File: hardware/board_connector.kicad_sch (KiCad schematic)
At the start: 3 parts, among them J6 61301611821, J7 PH1-08-UA, J8 PRT-09279

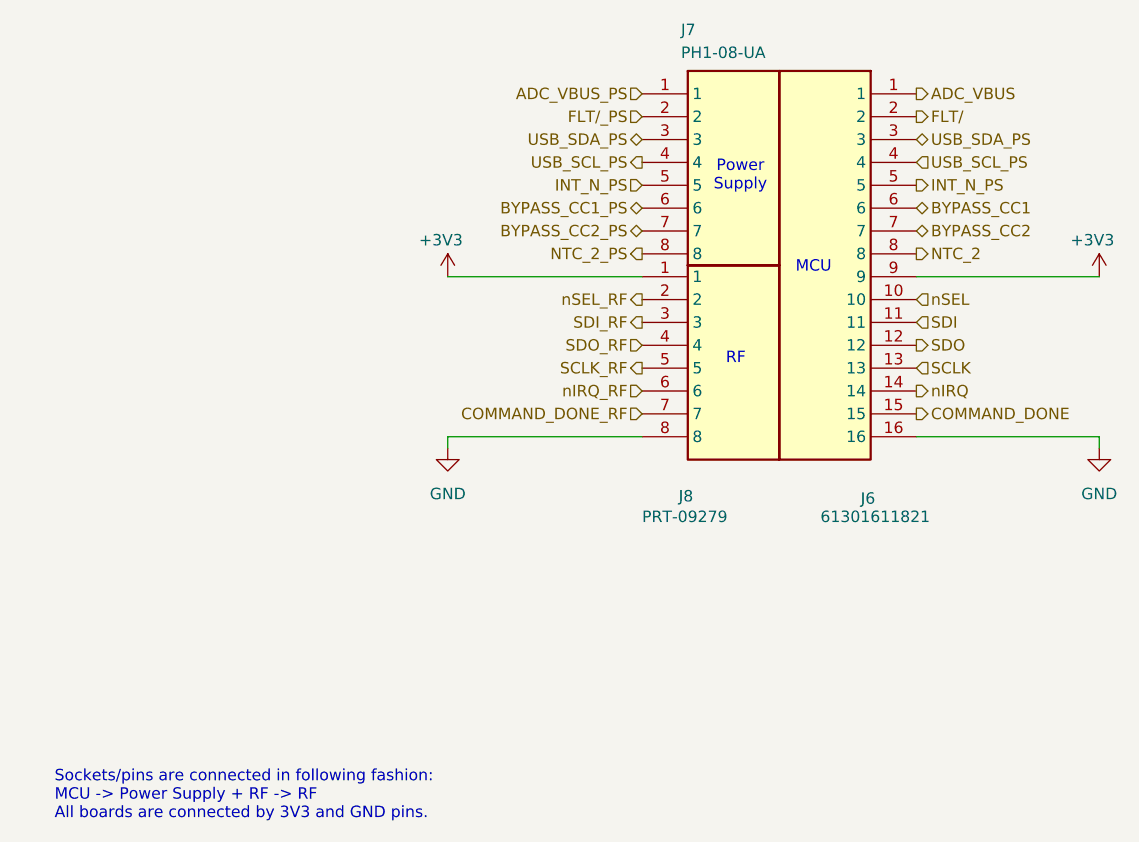
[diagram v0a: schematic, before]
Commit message: Fixed MOS and board connector
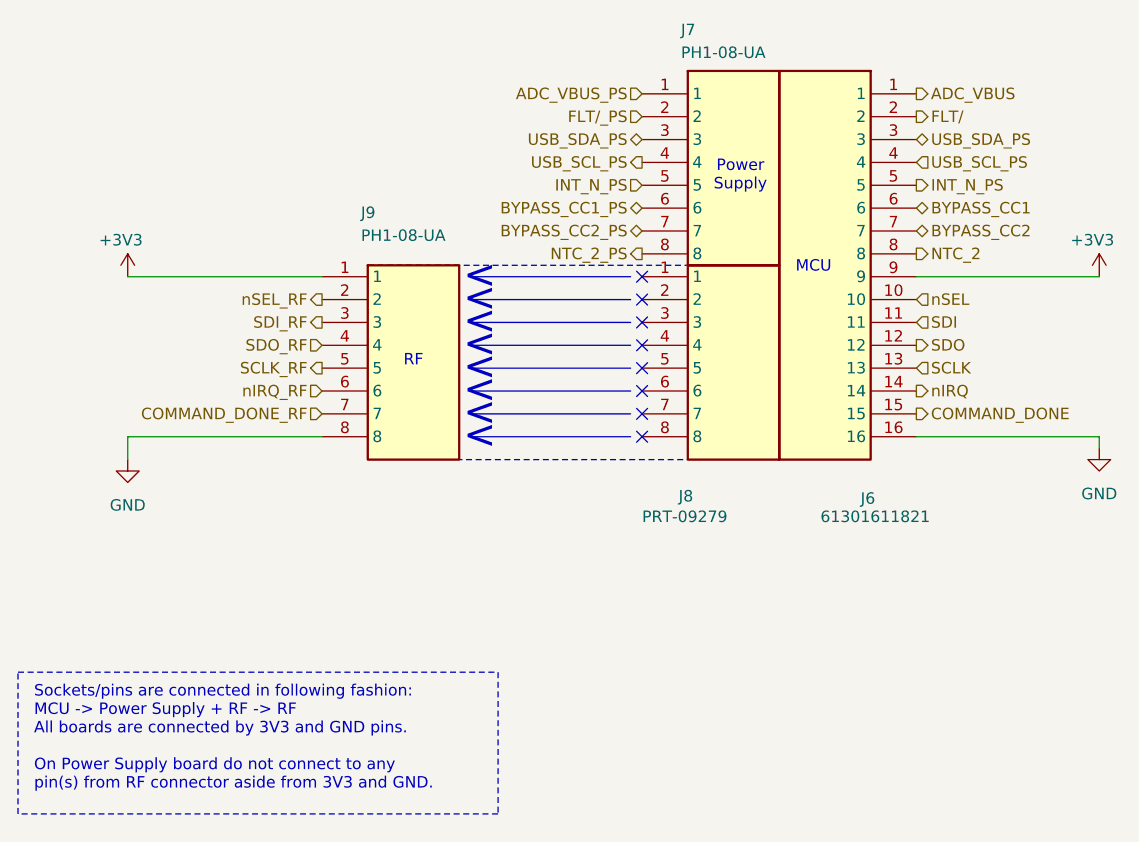
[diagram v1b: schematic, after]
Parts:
- added J9: PH1-08-UA, HDRV8W64P0X254_1X8_2032X250X888P, symbol SamacSys_Parts:PH1-08-UA
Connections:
- net +3V3: now also J9.1; no longer J8.1
- net COMMAND_DONE_RF: now also J9.7; no longer J8.7
- net GND: now also J9.8; no longer J8.8
- net SCLK_RF: now also J9.5; no longer J8.5
- net SDI_RF: now also J9.3; no longer J8.3
- net SDO_RF: now also J9.4; no longer J8.4
- net nIRQ_RF: now also J9.6; no longer J8.6
- net nSEL_RF: now also J9.2; no longer J8.2
- no-connect marks 0 -> 8
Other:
- note added: "<"
- note added: "Sockets/pins are connected in following fashion: MCU -> Power Supply + RF -> RF All boards are connected by 3V3 and GND pins. On Power Supply board do not connect to any pin(s) from RF connector aside from 3V3 and GND."
- note removed: "Sockets/pins are connected in following fashion: MCU -> Power Supply + RF -> RF All boards are connected by 3V3 and GND pins."

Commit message: prevention save
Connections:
- net INT_N_PS: no longer J6.5
- net USB_SCL_PS: no longer J6.4
- net USB_SDA_PS: no longer J6.3
- new net INT_N: J6.5
- new net USB_SCL: J6.4
- new net USB_SDA: J6.3
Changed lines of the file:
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@@
 		)
 	)
-	(hierarchical_label "INT_N_PS"
+	(hierarchical_label "INT_N"
 		(shape output)
 		(at 121.92 49.53 0)
@@
 		)
 	)
-	(hierarchical_label "USB_SDA_PS"
+	(hierarchical_label "USB_SDA"
 		(shape bidirectional)
 		(at 121.92 44.45 0)
@@
 		)
 	)
-	(hierarchical_label "USB_SCL_PS"
+	(hierarchical_label "USB_SCL"
 		(shape input)
 		(at 121.92 46.99 0)
